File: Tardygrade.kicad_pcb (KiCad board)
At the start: 2 copper layers, 50 x 50 mm, 25 parts, among them J1 Conn_01x03, J2 Conn_01x03, J3 Conn_01x03, J4 Conn_01x03, Q1 FET, Q2 FET, U1 MCP1642B, U2 HUZZAH32, U3 Tinypico, U4 HallSwitch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

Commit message: Changed some GPIOs. Minor edits.
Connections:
- R1 pad 1: VBAT_Source -> 3V3_Source
- U1 pad 1: PWR_EN -> Net-(U1-Pad1)
- U2 pad 22: HallRear -> HallFront
- U2 pad 23: LidarFront -> HallRear
- U2 pad 24: LidarRear -> HallRight
- U2 pad 7: HallRight -> LidarFront
- U2 pad 8: HallFront -> LidarRear
- U3 pad 13: HallRear -> HallFront
- U3 pad 14: LidarFront -> HallRear
- U3 pad 15: LidarRear -> HallRight
- U3 pad 3: HallRight -> LidarFront
- U3 pad 4: HallFront -> LidarRear
- U3 pad 6: SCK -> ServoRear
- U3 pad 7: MOSI -> SCK
- U3 pad 8: ServoRear -> MOSI
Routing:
- net PWR_EN: track 42.3 -> 16.5 mm, vias 1 -> 0
- net LidarRear: track 13.2 -> 34.4 mm, vias 0 -> 1
- net HallFront: track 6.86 -> 27.7 mm
- net LidarFront: track 18.9 -> 33.8 mm, vias 0 -> 1
- net 3V3_Source: track 63.0 -> 68.9 mm
- net VBAT_Source: track 14.2 -> 9.10 mm
- net ServoRear: track 41.1 -> 36.0 mm
- net HallRight: track 15.1 -> 19.9 mm
- net MOSI: track 29.3 -> 24.8 mm
- net HallRear: track 13.3 -> 10.6 mm
- net SCK: track 25.2 -> 22.7 mm

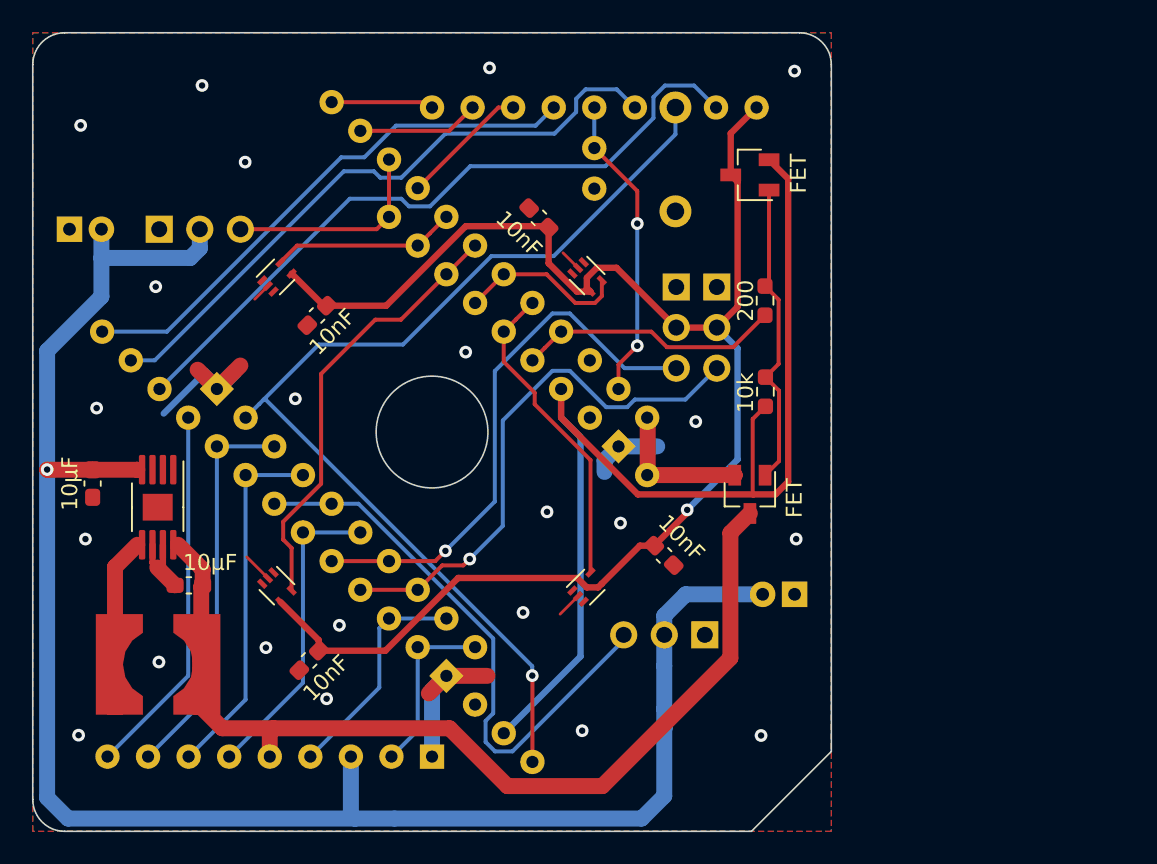
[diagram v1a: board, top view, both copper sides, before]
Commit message: Changed cap values for hall switches
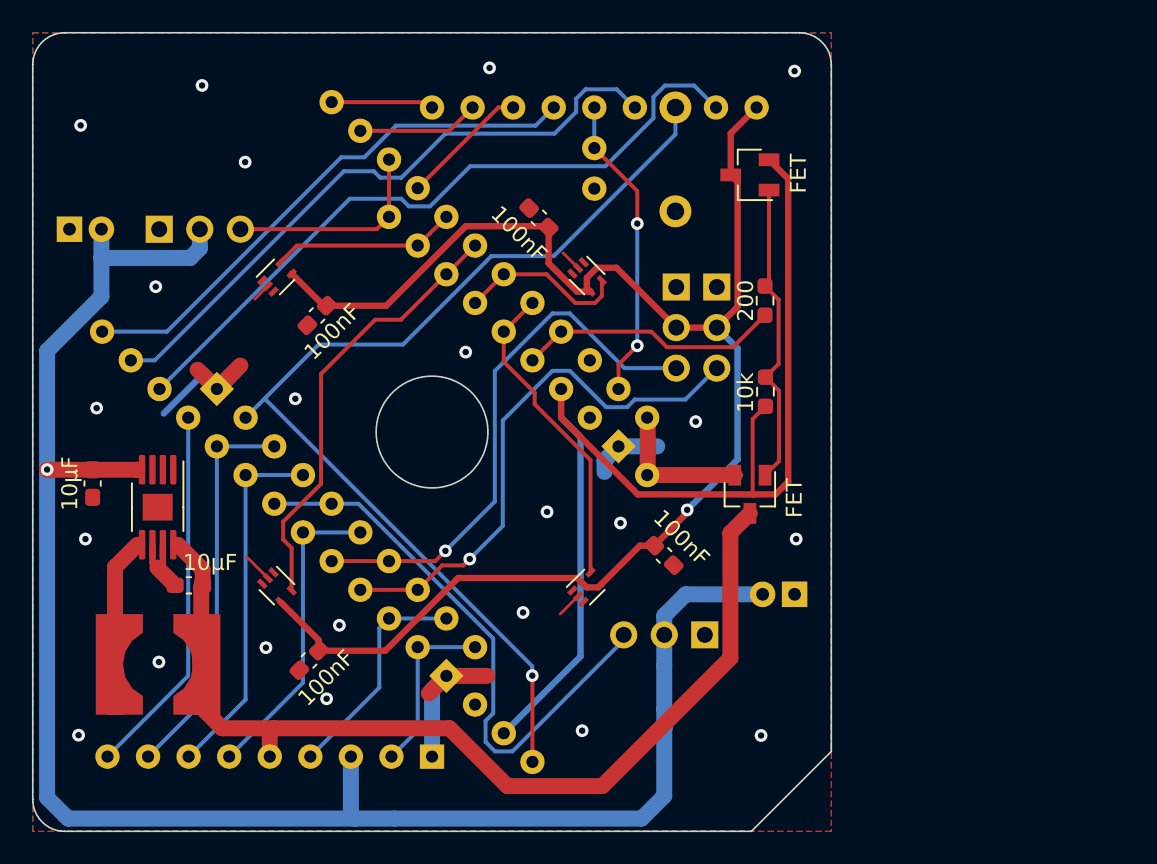
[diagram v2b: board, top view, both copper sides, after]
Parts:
- C11, C5, C7, C9: value 10nF -> 100nF

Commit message: v0.4 update
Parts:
- removed Q1, Q2: FET, 222footprints:SOT-23_Handsolder
- removed R2: 200, Resistor_SMD:R_0603_1608Metric_Pad0.98x0.95mm_HandSolder
- added J5: Conn_01x03_Male, Connector_PinHeader_2.54mm:PinHeader_1x03_P2.54mm_Vertical, B.Cu at (121.9, 106.7)
- C1, C2, L1, U1: moved to B.Cu
- R1: footprint Resistor_SMD:R_0603_1608Metric_Pad0.98x0.95mm_HandSolder -> Resistor_SMD:R_0201_0603Metric_Pad0.64x0.40mm_HandSolder
- moved C2 44.4 mm to (122.0, 93.2)
- moved L1 39.1 mm to (119.5, 101.0)
- moved U1 38.0 mm to (119.5, 94.6)
- moved C1 34.9 mm to (117.0, 96.0), turned to 90 degrees
- moved R1 22.3 mm to (142.2, 104.0), turned to 0 degrees
- moved J3 7.10 mm to (117.8, 88.9)
- moved J4 7.10 mm to (115.3, 88.9)
- moved C4 6.68 mm to (120.7, 116.8)
- moved C5 6.34 mm to (108.2, 108.2), turned to 225 degrees
- moved C7 5.11 mm to (111.3, 88.9)
- moved C9 4.63 mm to (88.9, 111.2), turned to 135 degrees
- moved C3 3.48 mm to (79.3, 83.8)
- moved C11 1.14 mm to (91.9, 91.9)
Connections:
- net VBAT_Source renamed VBAT
- C1 pad 1: VBAT_Drain -> VBAT_Rail
- C11 pad 1: 3V3_Drain -> 3V3_Rail
- C5 pad 1: 3V3_Drain -> 3V3_Rail
- C7 pad 1: 3V3_Drain -> 3V3_Rail
- C9 pad 1: 3V3_Drain -> 3V3_Rail
- J3 pad 2: 3V3_Drain -> 3V3_Rail
- J4 pad 2: 3V3_Drain -> 3V3_Rail
- L1 pad 2: VBAT_Drain -> VBAT_Rail
- R1 pad 1: 3V3_Source -> GND
- R1 pad 2: Net-(Q1-Pad1) -> VBAT_Rail
- U1 pad 1: Net-(U1-Pad1) -> BOOST_EN
- U1 pad 8: VBAT_Drain -> VBAT_Rail
- U2 pad 2: 3V3_Source -> 3V3_Rail
- U2 pad 25: PWR_EN -> BOOST_EN
- U3 pad 16: PWR_EN -> BOOST_EN
- U3 pad 17: 3V3_Source -> 3V3_Rail
- U4 pad 4: 3V3_Drain -> 3V3_Rail
- U5 pad 4: 3V3_Drain -> 3V3_Rail
- U6 pad 4: 3V3_Drain -> 3V3_Rail
- U7 pad 4: 3V3_Drain -> 3V3_Rail
- X1 pad 1: 3V3_Drain -> 3V3_Rail
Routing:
- net 3V3_Drain: track 95.3 -> 0.00 mm, vias 1 -> 0
- net 3V3_Rail: track 0.00 -> 76.8 mm
- net 3V3_Source: track 68.9 -> 0.00 mm
- net Reset: track 65.6 -> 0.00 mm, vias 1 -> 0
- net VBAT_Drain: track 63.2 -> 0.00 mm
- net RX: track 44.5 -> 0.00 mm
- net TX: track 39.9 -> 0.00 mm
- net ServoRear: track 36.0 -> 0.00 mm
- net GND: track 38.7 -> 4.51 mm, vias 22 -> 0
- net LidarRear: track 34.4 -> 0.16 mm, vias 1 -> 0
- net LidarFront: track 33.8 -> 0.00 mm, vias 1 -> 0
- net VBAT_Rail: track 0.00 -> 31.6 mm
- net HallFront: track 27.7 -> 0.00 mm
- net HallRight: track 19.9 -> 0.00 mm
- net Net-(Q1-Pad1): track 19.4 -> 0.00 mm
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- added copper zone on B.Cu, net 5V_Rail
- added copper zone on B.Cu, net Net-(L1-Pad1)
- added copper zone on B.Cu, net VBAT_Rail
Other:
- board text added: "Tardygrade v0.4"
- board text removed: "Tardygrade v0.31"

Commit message: more work on v0.4
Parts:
- moved J5 14.8 mm to (115.6, 93.3), turned to 270 degrees
- moved R1 13.3 mm to (129.5, 108.3)
- moved C2 6.60 mm to (122.0, 99.8)
- moved U1 6.35 mm to (119.5, 101.0)
- moved L1 6.35 mm to (119.5, 107.3)
- moved C1 5.84 mm to (117.0, 101.9)
- moved C4 3.21 mm to (118.7, 119.4)
- moved J2 2.00 mm to (110.0, 112.7)
- moved J3 0.73 mm to (117.5, 89.5)
- moved J4 0.73 mm to (114.9, 89.5)
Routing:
- net 5V_Rail: track 102.0 -> 0.00 mm
- net 3V3_Rail: track 76.8 -> 43.3 mm
- net VBAT_Rail: track 31.6 -> 0.00 mm
- net VBAT: track 16.2 -> 0.00 mm
- net Net-(L1-Pad1): track 14.1 -> 0.00 mm
- net GND: track 4.51 -> 0.00 mm

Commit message: v.04 update3
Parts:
- R1: footprint Resistor_SMD:R_0201_0603Metric_Pad0.64x0.40mm_HandSolder -> Resistor_SMD:R_0603_1608Metric_Pad0.98x0.95mm_HandSolder
- moved R1 16.3 mm to (113.3, 106.6), turned to 90 degrees
- moved C3 3.75 mm to (81.3, 80.6)
- moved J1 2.00 mm to (90.0, 87.3)
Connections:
- U1 pad 1: BOOST_EN -> 3V3_Rail
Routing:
- net 5V_Rail: track 0.00 -> 137.4 mm
- net 3V3_Rail: track 43.3 -> 113.4 mm
- net Reset: track 0.00 -> 69.3 mm
- net RX: track 0.00 -> 41.2 mm
- net TX: track 0.00 -> 35.6 mm
- net LidarFront: track 0.00 -> 31.9 mm
- net LidarRear: track 0.16 -> 30.3 mm
- net ServoRear: track 0.00 -> 26.0 mm
- net VBAT_Rail: track 0.00 -> 22.5 mm, vias 0 -> 1
- net HallRight: track 0.00 -> 19.9 mm
- net VBAT: track 0.00 -> 10.9 mm
- net GND: track 0.00 -> 10.7 mm, vias 0 -> 27
- net EN: track 0.00 -> 10.6 mm
- net HallRear: track 0.00 -> 9.33 mm
- net Net-(L1-Pad1): track 0.00 -> 4.77 mm
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- removed copper zone on B.Cu, net 5V_Rail
- removed copper zone on B.Cu, net Net-(L1-Pad1)
- removed copper zone on B.Cu, net VBAT_Rail

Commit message: v0.4 update 4
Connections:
- X1 pad 1: 3V3_Rail -> VBAT_Rail
- X1 pad 12: 5V_Rail -> DAC1
- X1 pad 13: DAC1 -> GPIO36
- X1 pad 14: VBAT_Drain -> SCK
- X1 pad 15: GPIO36 -> MOSI
- X1 pad 16: SCK -> MISO
- X1 pad 17: MOSI -> GPIO21
- X1 pad 2: RX -> 3V3_Rail
- X1 pad 3: Reset -> 5V_Rail
- X1 pad 4: TX -> Reset
- X1 pad 6: GPIO21 -> TX
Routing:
- net 5V_Rail: track 137.4 -> 108.6 mm
- net HallFront: track 2.54 -> 28.7 mm
- net GND: track 10.7 -> 28.1 mm, vias 27 -> 34
- net Reset: track 69.3 -> 86.5 mm
- net VBAT_Rail: track 22.5 -> 39.6 mm
- net GPIO21: track 34.5 -> 27.8 mm
- net SCK: track 22.7 -> 28.9 mm
- net Net-(L1-Pad1): track 4.77 -> 9.64 mm
- net RX: track 41.2 -> 37.9 mm
- net MOSI: track 24.8 -> 27.8 mm
- net 3V3_Rail: track 113.4 -> 110.7 mm
- net MISO: track 23.3 -> 24.8 mm
- net DAC1: track 14.3 -> 13.2 mm
- net GPIO36: track 19.5 -> 20.5 mm
- net TX: track 35.6 -> 36.1 mm
- added copper zone on B.Cu, net 5V_Rail
- added copper zone on B.Cu, net Net-(L1-Pad1)
- added copper zone on B.Cu, net VBAT_Rail

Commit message: v0.4 update 5
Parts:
- R1: value 10k -> 20k
- moved R1 0.82 mm to (114.0, 106.9)
- moved C1 0.35 mm to (117.0, 102.2)
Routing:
- net GND: track 28.1 -> 21.5 mm, vias 34 -> 33
- net 5V_Rail: track 108.6 -> 111.0 mm
- net 3V3_Rail: track 110.7 -> 111.4 mm
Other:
- board text added: "Off/On"

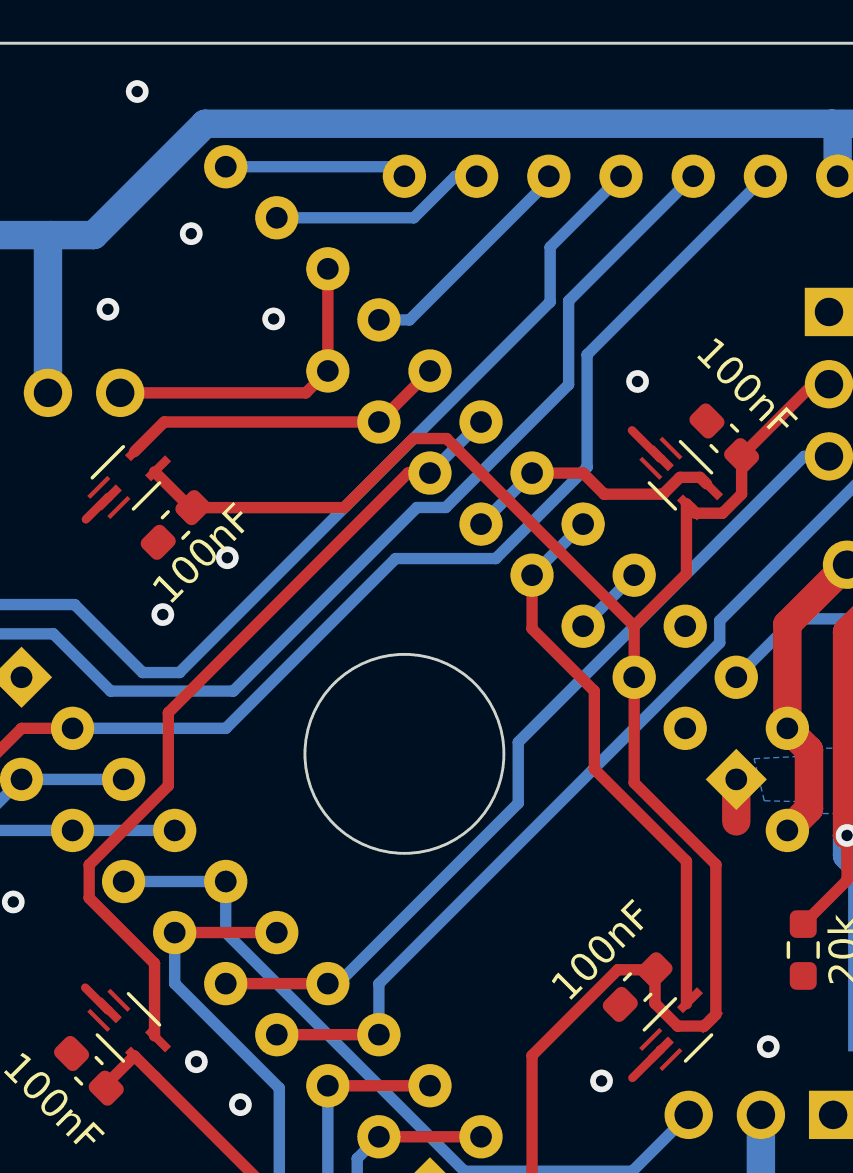
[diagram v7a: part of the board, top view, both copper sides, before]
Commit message: Reassigned GPIO12 -> GPIO32 on Adafruit. New board v0.41
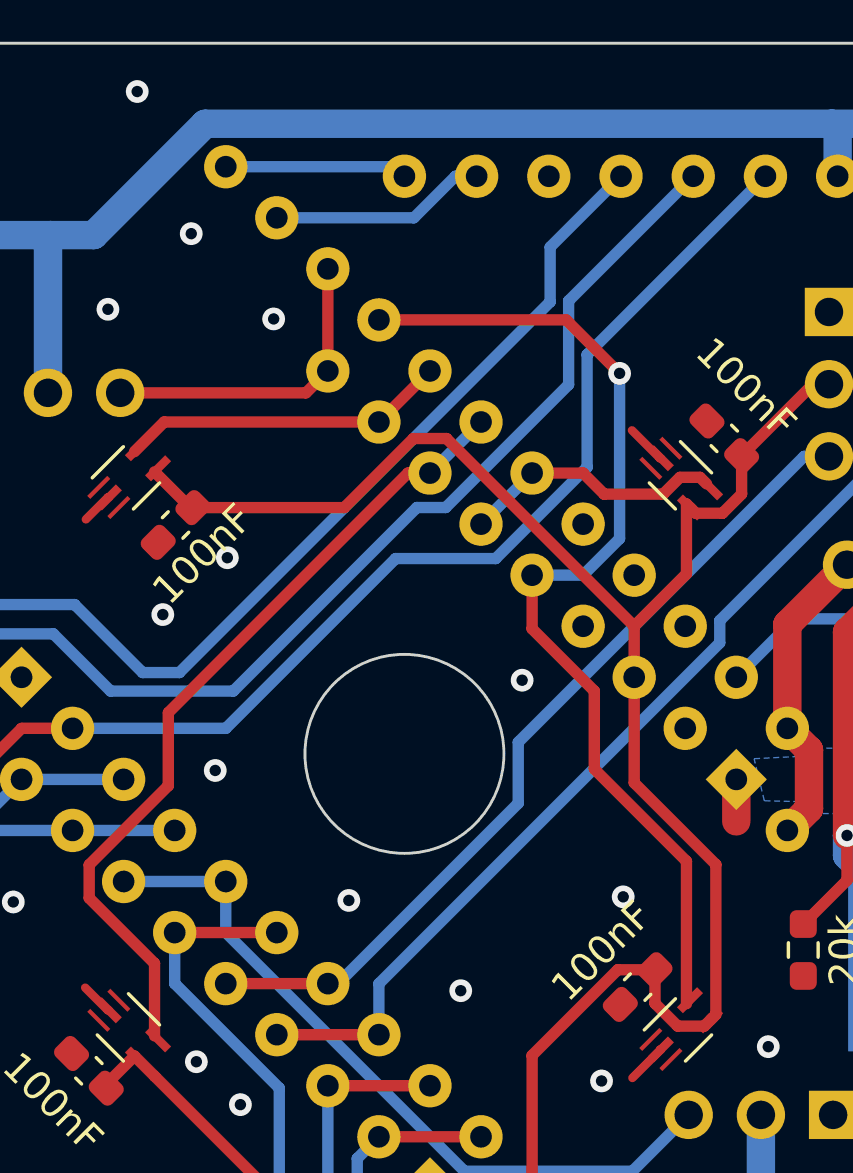
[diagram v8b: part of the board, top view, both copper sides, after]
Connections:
- U2 pad 20: GPIO32 -> HallRight
- U2 pad 24: HallRight -> Net-(U2-Pad24)
- U2 pad 25: BOOST_EN -> Net-(U2-Pad25)
- U3 pad 16: BOOST_EN -> Net-(U3-Pad16)
- X1 pad 7: GPIO32 -> Net-(X1-Pad7)
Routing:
- net HallRight: track 19.9 -> 36.0 mm, vias 0 -> 1
- net GPIO32: track 8.16 -> 0.00 mm
- net BOOST_EN: track 2.54 -> 0.00 mm
- net GND: vias 33 -> 37
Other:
- board text added: "Tardygrade v0.41"
- board text removed: "Tardygrade v0.4"
